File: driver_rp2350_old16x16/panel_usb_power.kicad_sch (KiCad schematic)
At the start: 4 parts, among them J1 Conn_01x04, U39 AP2112K-3.3

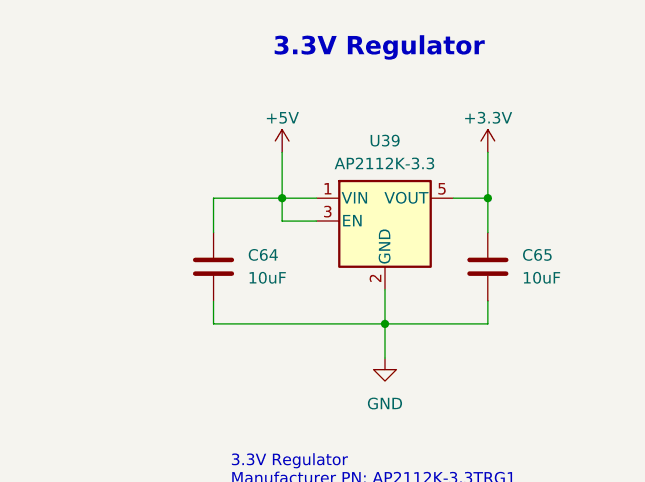
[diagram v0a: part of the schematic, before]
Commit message: Worked on new 18x18 led version of rp2350 design.
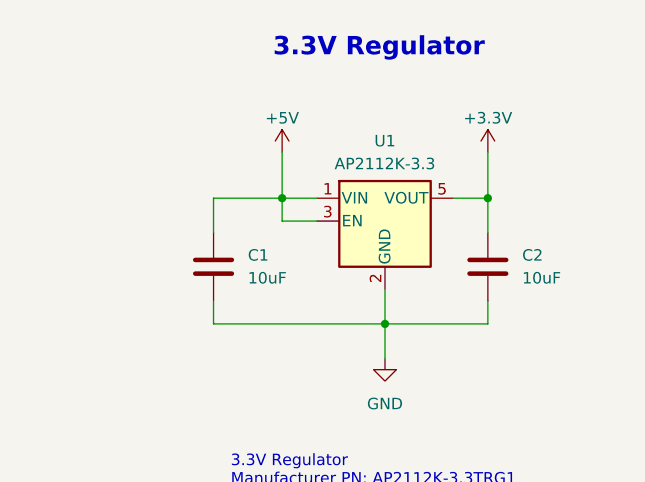
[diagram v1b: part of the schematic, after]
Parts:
- C1: renamed from C64; footprint Capacitor_SMD:C_0402_1005Metric -> panel_custom:C_0402_1005Metric
- C2: renamed from C65; footprint Capacitor_SMD:C_0402_1005Metric -> panel_custom:C_0402_1005Metric
- J1: footprint panel_custom:JST_SH_BM04B-SRSS-TB_1x04-1MP_P1.00mm_Vertical -> panel_custom:JST_SH_SM04B-SRSS-TB_1x04-1MP_P1.00mm_Horizontal
- renumbered U39 to U1
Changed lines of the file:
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@@
 		(dnp no)
 		(fields_autoplaced yes)
-		(property "Reference" "#PWR0109"
+		(property "Reference" "#PWR077"
 			(at 100.965 59.69 0)
 			(effects
@@
 			(project "driver_rp2350"
 				(path "/1e634561-32a0-4ffa-9d4f-e93f355464d5/e614504e-e15b-412a-a899-de4ba0827a39"
-					(reference "#PWR0109")
+					(reference "#PWR077")
 					(unit 1)
 				)
@@
 		(dnp no)
 		(fields_autoplaced yes)
-		(property "Reference" "#PWR0112"
+		(property "Reference" "#PWR075"
 			(at 226.06 44.45 0)
 			(effects
@@
 			(project "driver_rp2350"
 				(path "/1e634561-32a0-4ffa-9d4f-e93f355464d5/e614504e-e15b-412a-a899-de4ba0827a39"
-					(reference "#PWR0112")
+					(reference "#PWR075")
 					(unit 1)
 				)
@@
 		(on_board yes)
 		(dnp no)
-		(property "Reference" "#PWR0108"
+		(property "Reference" "#PWR018"
 			(at 100.965 48.895 0)
 			(effects
@@
 			(project "driver_rp2350"
 				(path "/1e634561-32a0-4ffa-9d4f-e93f355464d5/e614504e-e15b-412a-a899-de4ba0827a39"
-					(reference "#PWR0108")
+					(reference "#PWR018")
 					(unit 1)
 				)
@@
 		(on_board yes)
 		(dnp no)
-		(property "Reference" "#PWR0110"
+		(property "Reference" "#PWR074"
 			(at 203.2 44.45 0)
 			(effects
@@
 			(project "driver_rp2350"
 				(path "/1e634561-32a0-4ffa-9d4f-e93f355464d5/e614504e-e15b-412a-a899-de4ba0827a39"
-					(reference "#PWR0110")
+					(reference "#PWR074")
 					(unit 1)
 				)
@@
 		(dnp no)
 		(fields_autoplaced yes)
-		(property "Reference" "C64"
+		(property "Reference" "C1"
 			(at 199.39 52.07 0)
 			(effects
@@
 			)
 		)
-		(property "Footprint" "Capacitor_SMD:C_0402_1005Metric"
+		(property "Footprint" "panel_custom:C_0402_1005Metric"
 			(at 196.5452 57.15 0)
 			(effects
@@
 			(project "driver_rp2350"
 				(path "/1e634561-32a0-4ffa-9d4f-e93f355464d5/e614504e-e15b-412a-a899-de4ba0827a39"
-					(reference "C64")
+					(reference "C1")
 					(unit 1)
 				)
@@
 			)
 		)
-		(property "Footprint" "panel_custom:JST_SH_BM04B-SRSS-TB_1x04-1MP_P1.00mm_Vertical"
+		(property "Footprint" "panel_custom:JST_SH_SM04B-SRSS-TB_1x04-1MP_P1.00mm_Horizontal"
 			(at 73.66 49.53 0)
 			(effects
@@
 		(dnp no)
 		(fields_autoplaced yes)
-		(property "Reference" "C65"
+		(property "Reference" "C2"
 			(at 229.87 52.07 0)
 			(effects
@@
 			)
 		)
-		(property "Footprint" "Capacitor_SMD:C_0402_1005Metric"
+		(property "Footprint" "panel_custom:C_0402_1005Metric"
 			(at 227.0252 57.15 0)
 			(effects
@@
 			(project "driver_rp2350"
 				(path "/1e634561-32a0-4ffa-9d4f-e93f355464d5/e614504e-e15b-412a-a899-de4ba0827a39"
-					(reference "C65")
+					(reference "C2")
 					(unit 1)
 				)
@@
 		(dnp no)
 		(fields_autoplaced yes)
-		(property "Reference" "U39"
+		(property "Reference" "U1"
 			(at 214.63 39.37 0)
 			(effects
@@
 			(project "driver_rp2350"
 				(path "/1e634561-32a0-4ffa-9d4f-e93f355464d5/e614504e-e15b-412a-a899-de4ba0827a39"
-					(reference "U39")
+					(reference "U1")
 					(unit 1)
 				)
@@
 		(dnp no)
 		(fields_autoplaced yes)
-		(property "Reference" "#PWR0111"
+		(property "Reference" "#PWR076"
 			(at 214.63 69.85 0)
 			(effects
@@
 			(project "driver_rp2350"
 				(path "/1e634561-32a0-4ffa-9d4f-e93f355464d5/e614504e-e15b-412a-a899-de4ba0827a39"
-					(reference "#PWR0111")
-					(unit 1)
-				)
+					(reference "#PWR076")
+					(unit 1)
+				)
